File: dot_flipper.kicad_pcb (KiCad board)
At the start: 4 copper layers, 10.2 x 71 mm, 65 parts, among them J1 VM_i, J10 SEROUT, J11 SRCLK_o, J12 LATCH_o, J13 SLEEP_o, J14 GND_o, J2 VCC_i, J3 SERIN, J4 SRCLK_i, J5 LATCH_i, J6 SLEEP_i, J7 GND_i, J8 VM_o, J9 VCC_o, U1 SN74LVC1G04DCKR, U10 SN74LVC1G04DCKR, U11 DRV8837CDSGR, U12 CDSOT236-T05C, U13 SN74LVC1G04DCKR, U14 DRV8837CDSGR, U15 SN74LVC1G04DCKR, U16 DRV8837CDSGR, U17 SN74LVC1G04DCKR, U18 DRV8837CDSGR, U2 DRV8837CDSGR, U3 7_flip_dots, U4 SN74HC595PWR, U5 SN74LVC1G04DCKR, U6 DRV8837CDSGR, U7 SN74LVC1G04DCKR, U8 DRV8837CDSGR, U9 CDSOT236-T05C

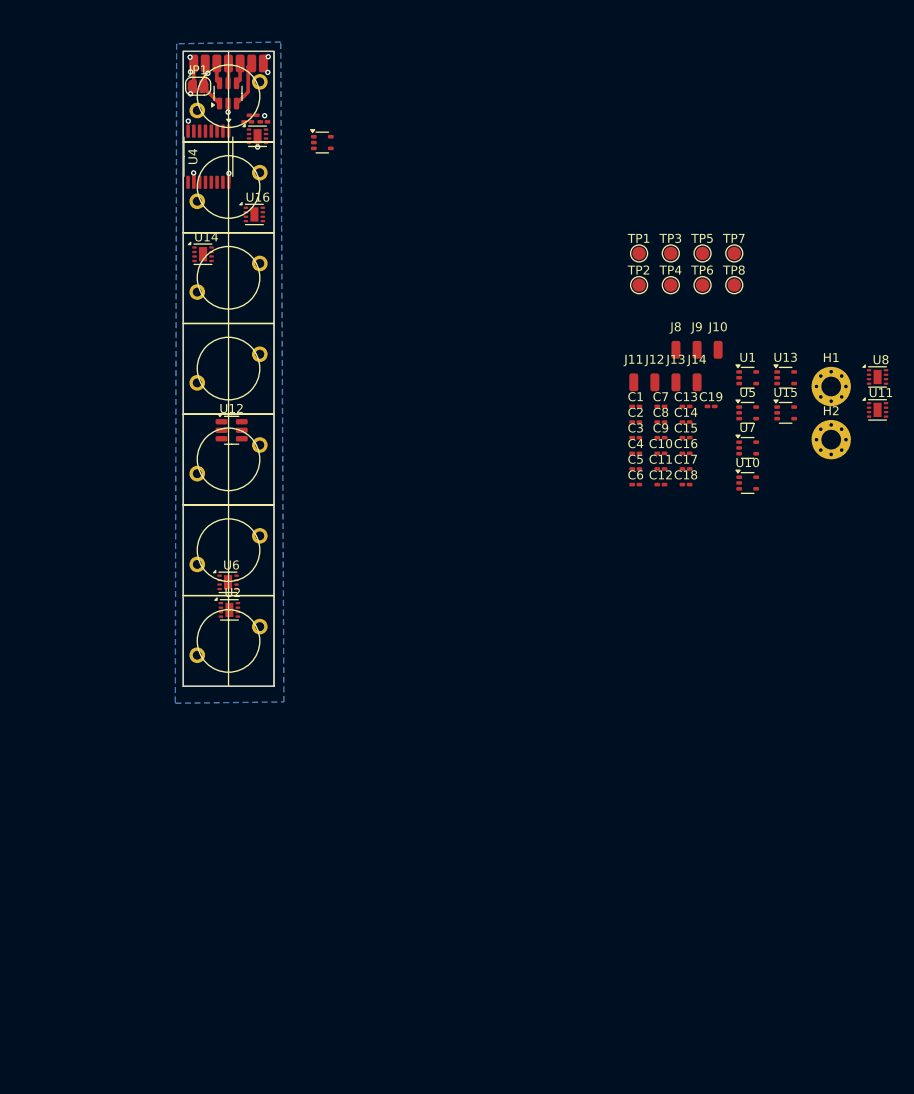
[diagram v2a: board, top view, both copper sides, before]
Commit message: Started PCB layout
Components in vaguely the correct area
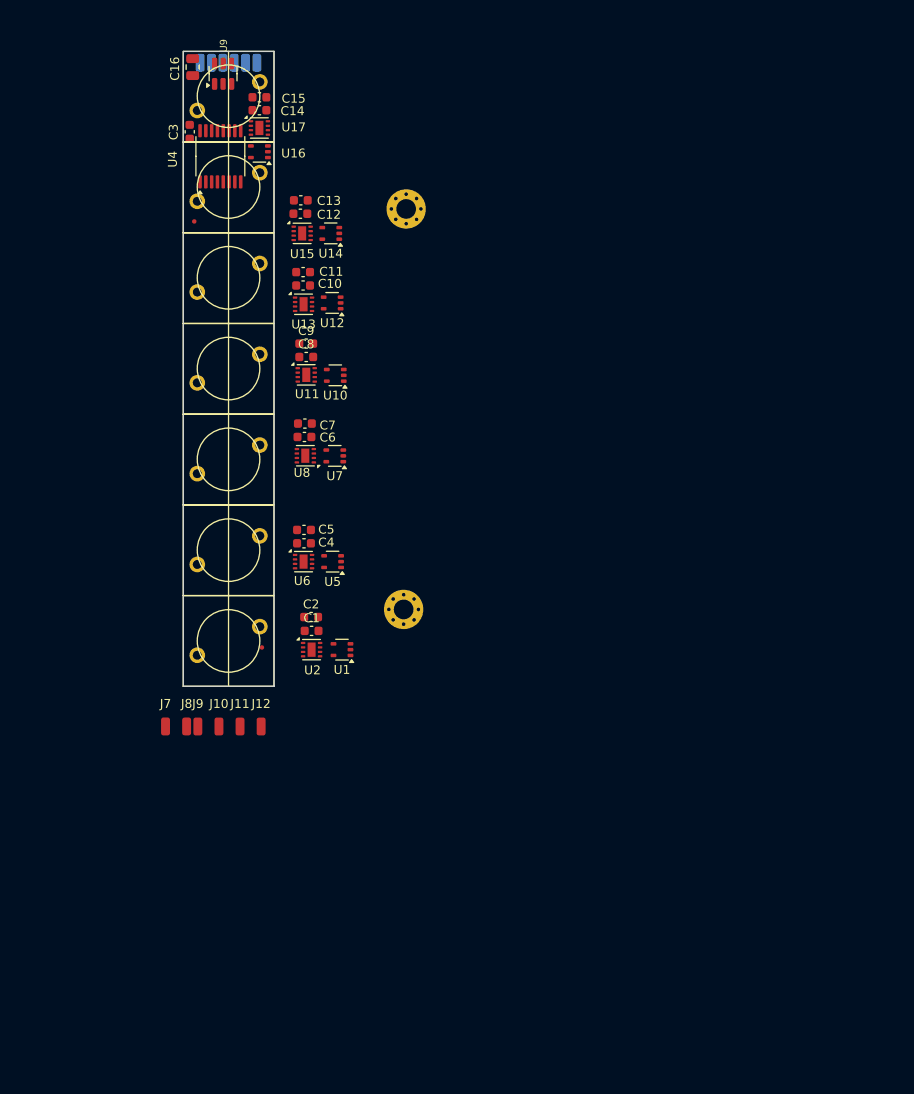
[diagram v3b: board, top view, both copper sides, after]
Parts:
- removed the C1 at (92.6, 59.6)
- removed the C11 at (95.4, 66.6)
- removed the C14 at (98.2, 61.4)
- removed C17, C20: 100n/16V, Capacitor_SMD:C_0201_0603Metric_Pad0.64x0.40mm_HandSolder
- removed the C5 at (92.6, 66.6)
- removed the C8 at (95.4, 61.4)
- removed the J7 at (50.9, 21.2)
- removed the J8 at (97.1, 53.3)
- removed JP1: SolderJumper_2_Open, Jumper:SolderJumper-2_P1.3mm_Open_RoundedPad1.0x1.5mm
- removed TP1: SEROUT, TestPoint:TestPoint_Pad_D1.5mm
- removed TP2: SRCLK, TestPoint:TestPoint_Pad_D1.5mm
- removed TP3: LATCH, TestPoint:TestPoint_Pad_D1.5mm
- removed TP4: SLEEP, TestPoint:TestPoint_Pad_D1.5mm
- removed TP5: SERIN, TestPoint:TestPoint_Pad_D1.5mm
- removed TP6: VCC, TestPoint:TestPoint_Pad_D1.5mm
- removed TP7, TP8: GND, TestPoint:TestPoint_Pad_D1.5mm
- removed the U12 at (47.4, 62.3)
- added C16: 4u7, Capacitor_SMD:C_0805_2012Metric, F.Cu at (43.0, 21.6)
- added FID1: Fiducial, Fiducial:Fiducial_0.5mm_Mask1.5mm, F.Cu at (43.2, 38.9)
- added FID2: Fiducial, Fiducial:Fiducial_0.5mm_Mask1.5mm, F.Cu at (50.8, 86.6)
- C1: renamed from C2; footprint Capacitor_SMD:C_0201_0603Metric_Pad0.64x0.40mm_HandSolder -> Capacitor_SMD:C_0603_1608Metric
- C10: renamed from C15; footprint Capacitor_SMD:C_0201_0603Metric_Pad0.64x0.40mm_HandSolder -> Capacitor_SMD:C_0603_1608Metric
- C11: renamed from C16; footprint Capacitor_SMD:C_0201_0603Metric_Pad0.64x0.40mm_HandSolder -> Capacitor_SMD:C_0603_1608Metric
- C12: renamed from C18; footprint Capacitor_SMD:C_0201_0603Metric_Pad0.64x0.40mm_HandSolder -> Capacitor_SMD:C_0603_1608Metric
- C13: renamed from C19; footprint Capacitor_SMD:C_0201_0603Metric_Pad0.64x0.40mm_HandSolder -> Capacitor_SMD:C_0603_1608Metric
- C14: renamed from C21; footprint Capacitor_SMD:C_0201_0603Metric_Pad0.64x0.40mm_HandSolder -> Capacitor_SMD:C_0603_1608Metric
- C15: renamed from C22; footprint Capacitor_SMD:C_0201_0603Metric_Pad0.64x0.40mm_HandSolder -> Capacitor_SMD:C_0603_1608Metric
- C2: renamed from C3; footprint Capacitor_SMD:C_0201_0603Metric_Pad0.64x0.40mm_HandSolder -> Capacitor_SMD:C_0603_1608Metric
- C3: renamed from C4; footprint Capacitor_SMD:C_0201_0603Metric_Pad0.64x0.40mm_HandSolder -> Capacitor_SMD:C_0603_1608Metric
- C4: renamed from C6; footprint Capacitor_SMD:C_0201_0603Metric_Pad0.64x0.40mm_HandSolder -> Capacitor_SMD:C_0603_1608Metric
- C5: renamed from C7; footprint Capacitor_SMD:C_0201_0603Metric_Pad0.64x0.40mm_HandSolder -> Capacitor_SMD:C_0603_1608Metric
- C6: renamed from C9; footprint Capacitor_SMD:C_0201_0603Metric_Pad0.64x0.40mm_HandSolder -> Capacitor_SMD:C_0603_1608Metric
- C7: renamed from C10; footprint Capacitor_SMD:C_0201_0603Metric_Pad0.64x0.40mm_HandSolder -> Capacitor_SMD:C_0603_1608Metric
- C8: renamed from C12; footprint Capacitor_SMD:C_0201_0603Metric_Pad0.64x0.40mm_HandSolder -> Capacitor_SMD:C_0603_1608Metric
- C9: renamed from C13; footprint Capacitor_SMD:C_0201_0603Metric_Pad0.64x0.40mm_HandSolder -> Capacitor_SMD:C_0603_1608Metric
- J1: value VM_i -> VCC_i; moved to B.Cu
- J2: value VCC_i -> SERIN; moved to B.Cu
- J3: value SERIN -> SRCLK_i; moved to B.Cu
- J4: value SRCLK_i -> LATCH_i; moved to B.Cu
- J5: value LATCH_i -> SLEEP_i; moved to B.Cu
- J6: value SLEEP_i -> GND_i; moved to B.Cu
- moved J7 72.9 mm to (40.0, 95.4)
- moved J8 72.9 mm to (42.3, 95.4)
- moved U8 64.6 mm to (55.6, 65.1), turned to 180 degrees
- moved U11 64.1 mm to (55.7, 56.1)
- moved J10 62.2 mm to (45.9, 95.4)
- moved J11 62.2 mm to (48.3, 95.4)
- moved J12 62.2 mm to (50.7, 95.4)
- moved J9 62.2 mm to (43.6, 95.4)
- moved C3 61.5 mm to (42.7, 28.9), turned to -90 degrees
- moved U14 54.7 mm to (58.5, 40.3), turned to 180 degrees
- moved U1 54.7 mm to (59.7, 86.8), turned to 180 degrees
- moved C12 52.7 mm to (55.1, 38.1)
- moved H1 51.5 mm to (66.9, 37.5)
- moved H2 51.5 mm to (66.6, 82.3)
- moved U12 51.4 mm to (58.6, 48.0), turned to 180 degrees
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- renumbered J12 to J10, J13 to J11, J14 to J12, J9 to J7, J10 to J8, J11 to J9, U13 to U12, U14 to U13, U15 to U14, U16 to U15, U17 to U16, U18 to U17
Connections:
- C1 pad 1: VM -> VCC
- C10 pad 1: VM -> VCC
- C11 pad 1: VM -> VCC
- C12 pad 1: VM -> VCC
- C13 pad 1: VM -> VCC
- C14 pad 1: VM -> VCC
- C15 pad 1: VM -> VCC
- C2 pad 1: VM -> VCC
- C4 pad 1: VM -> VCC
- C5 pad 1: VM -> VCC
- C6 pad 1: VM -> VCC
- C7 pad 1: VM -> VCC
- C8 pad 1: VM -> VCC
- C9 pad 1: VM -> VCC
- J1 pad 1: VM -> VCC
- J2 pad 1: VCC -> /SERIN
- J3 pad 1: /SERIN -> /SRCLK
- J4 pad 1: /SRCLK -> /LATCH
- J5 pad 1: /LATCH -> /SLEEP
- J6 pad 1: /SLEEP -> GND
- U11 pad 1: VM -> VCC
- U13 pad 1: VM -> VCC
- U15 pad 1: VM -> VCC
- U17 pad 1: VM -> VCC
- U2 pad 1: VM -> VCC
- U6 pad 1: VM -> VCC
- U8 pad 1: VM -> VCC
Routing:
- net VCC: track 8.57 -> 0.00 mm, vias 4 -> 0
- net VM: track 5.52 -> 0.00 mm, vias 3 -> 0
- net /SLEEP: track 5.19 -> 0.00 mm
- net GND: track 4.35 -> 0.00 mm, vias 5 -> 0
- net /LATCH: track 2.38 -> 0.00 mm
- net /SERIN: track 2.34 -> 0.00 mm
- net /SRCLK: track 2.23 -> 0.00 mm
- added copper zone on In1.Cu, net GND
- removed copper zone on B.Cu, net GND
- removed copper zone on In1.Cu, net VM

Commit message: Update Mar 7 AM
- Implemented bus architecture to transfer data to second column, and transport signals down to each pixel
- simplified schematic more
- routed first (most difficult) pixel
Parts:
- added C17: 100n/16V, Capacitor_SMD:C_0603_1608Metric, F.Cu at (59.6, 89.0)
- added C18: 100n/16V, Capacitor_SMD:C_0603_1608Metric, F.Cu at (58.6, 79.1)
- added C19: 100n/16V, Capacitor_SMD:C_0603_1608Metric, F.Cu at (58.8, 67.3)
- added C20: 100n/16V, Capacitor_SMD:C_0603_1608Metric, F.Cu at (58.9, 58.3)
- added C21: 100n/16V, Capacitor_SMD:C_0603_1608Metric, F.Cu at (58.6, 50.2)
- added C22: 100n/16V, Capacitor_SMD:C_0603_1608Metric, F.Cu at (54.6, 41.7)
- added C23: 100n/16V, Capacitor_SMD:C_0603_1608Metric, F.Cu at (50.5, 31.7)
- added J2: SERIN, Connector_Wire:SolderWirePad_1x01_SMD_1x2mm, B.Cu at (55.6, 21.2)
- added J8: SEROUT, Connector_Wire:SolderWirePad_1x01_SMD_1x2mm, B.Cu at (61.9, 21.1)
- J10, J11, J12, J7, J8, J9: moved to B.Cu
- moved J7 75.6 mm to (54.3, 21.2), turned to 180 degrees
- moved J9 75.5 mm to (56.8, 21.1), turned to 180 degrees
- moved J10 75.3 mm to (58.1, 21.1), turned to 180 degrees
- moved J11 75.1 mm to (59.4, 21.1), turned to 180 degrees
- moved J12 75.0 mm to (60.7, 21.1), turned to 180 degrees
- moved J8 74.8 mm to (51.5, 21.2), turned to 180 degrees
- moved H1 33.5 mm to (37.1, 22.3)
- moved H2 28.9 mm to (38.3, 88.4)
- moved C12 4.09 mm to (58.3, 35.6)
- moved U14 3.90 mm to (54.6, 39.8)
- moved U15 3.16 mm to (54.6, 37.2)
- moved C14 2.77 mm to (48.6, 24.5), turned to 90 degrees
- moved C16 2.06 mm to (43.0, 23.7)
- moved U9 2.00 mm to (45.9, 24.3)
- moved U17 1.56 mm to (50.2, 26.9)
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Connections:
- J11 pad 1: /SLEEP -> /nOE
- J5 pad 1: /SLEEP -> /nOE
- U11 pad 7: /SLEEP -> VCC
- U13 pad 7: /SLEEP -> VCC
- U15 pad 7: /SLEEP -> VCC
- U17 pad 7: /SLEEP -> VCC
- U2 pad 7: /SLEEP -> unconnected-(U2-~{SLEEP}-Pad7)
- U4 pad 13: /SLEEP -> /nOE
- U6 pad 7: /SLEEP -> VCC
- U8 pad 7: /SLEEP -> VCC
- U9 pad 3: /SLEEP -> /nOE
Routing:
- net /OUT1: track 0.00 -> 57.2 mm, vias 0 -> 2
- net /OUT2: track 0.00 -> 39.7 mm, vias 0 -> 2
- net /OUT3: track 0.00 -> 26.5 mm, vias 0 -> 2
- net /LATCH: track 0.00 -> 23.1 mm, vias 0 -> 3
- net /SRCLK: track 0.00 -> 20.4 mm, vias 0 -> 3
- net /nOE: track 0.00 -> 19.6 mm, vias 0 -> 3
- net /OUT4: track 0.00 -> 19.1 mm, vias 0 -> 2
- net VCC: track 0.00 -> 18.6 mm, vias 0 -> 5
- net /SERIN: track 0.00 -> 16.5 mm, vias 0 -> 3
- net GND: track 0.00 -> 15.9 mm, vias 0 -> 10
- net /SEROUT: track 0.00 -> 12.9 mm, vias 0 -> 2
- net /OUT7: track 0.00 -> 12.0 mm
- net /OUT5: track 0.00 -> 6.80 mm, vias 0 -> 2
- net Net-(U17-OUT2): track 0.00 -> 6.25 mm
- net Net-(U17-OUT1): track 0.00 -> 6.25 mm
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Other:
- board text added: "1"
- board text added: "2"
- board text added: "3"
- board text added: "4"
- board text added: "5"
- board text added: "6"
- board text added: "7"

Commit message: Update Mar 7 PM
All pixels routed
7x7 variant created
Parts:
- removed H1, H2: MountingHole_Pad, MountingHole:MountingHole_2.2mm_M2_Pad_Via
- removed the J2 at (55.6, 21.2)
- removed the J8 at (61.9, 21.1)
- added FID3: Fiducial, Fiducial:Fiducial_0.5mm_Mask1.5mm, F.Cu at (43.4, 69.4)
- added J13: LATCH_o, Arans_Footprints:small_pad, F.Cu at (39.5, 21.6)
- added J14: SLEEP_o, Arans_Footprints:small_pad, F.Cu at (39.5, 22.3)
- C16: footprint Capacitor_SMD:C_0805_2012Metric -> Capacitor_SMD:C_0603_1608Metric
- J10, J11, J8, J9: footprint Connector_Wire:SolderWirePad_1x01_SMD_1x2mm -> Arans_Footprints:small_pad; moved to F.Cu
- J12: value GND_o -> SRCLK_o; footprint Connector_Wire:SolderWirePad_1x01_SMD_1x2mm -> Arans_Footprints:small_pad; moved to F.Cu
- J7: value VCC_o -> SERIN; footprint Connector_Wire:SolderWirePad_1x01_SMD_1x2mm -> Arans_Footprints:small_pad; moved to F.Cu
- moved J12 21.1 mm to (39.5, 21.0), turned to -90 degrees
- moved J7 14.8 mm to (39.5, 20.4), turned to -90 degrees
- moved U1 12.7 mm to (47.0, 87.9)
- moved C17 12.5 mm to (47.1, 90.0)
- moved C12 11.1 mm to (47.3, 36.5), turned to 180 degrees
- moved U7 10.2 mm to (50.1, 70.4)
- moved C19 10.0 mm to (50.1, 72.5), turned to 180 degrees
- moved U10 9.60 mm to (50.2, 60.1)
- moved C1 9.57 mm to (47.0, 82.6), turned to 180 degrees
- moved U2 9.49 mm to (47.0, 84.9), turned to -90 degrees
- moved C20 9.48 mm to (50.2, 62.2), turned to 180 degrees
- moved U5 9.24 mm to (50.1, 80.4)
- moved U12 8.96 mm to (49.8, 49.8)
- moved C18 8.91 mm to (50.3, 82.4), turned to 180 degrees
- moved C21 8.84 mm to (49.9, 51.9), turned to 180 degrees
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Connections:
- J12 pad 1: GND -> /SRCLK
- J7 pad 1: VCC -> /SERIN
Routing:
- net GND: track 15.9 -> 77.4 mm, vias 10 -> 67
- net VCC: track 18.6 -> 72.0 mm, vias 5 -> 26
- net /OUT4: track 19.1 -> 40.0 mm
- net /OUT5: track 6.80 -> 26.1 mm
- net /OUT6: track 1.48 -> 19.4 mm, vias 1 -> 2
- net /OUT2: track 39.7 -> 57.6 mm
- net /OUT3: track 26.5 -> 44.3 mm
- net /OUT1: track 57.2 -> 68.4 mm
- net Net-(U15-OUT1): track 0.00 -> 8.22 mm
- net Net-(U2-OUT1): track 0.00 -> 7.39 mm
- net Net-(U13-OUT1): track 0.00 -> 7.05 mm
- net Net-(U3C-b): track 0.00 -> 6.91 mm
- net Net-(U3B-b): track 0.00 -> 6.69 mm
- net Net-(U11-OUT1): track 0.00 -> 6.61 mm
- net Net-(U2-OUT2): track 0.00 -> 6.43 mm
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- added copper zone on B.Cu, net GND
- added copper zone on F.Cu, net GND
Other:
- board text added: "0V"
- board text added: "CLK"
- board text added: "EN"
- board text added: "F"
- board text added: "IN"
- board text added: "LATCH"
- board text added: "LI"
- board text added: "P"
- board text added: "Pe"
- board text added: "R"
- board text added: "VCC"
